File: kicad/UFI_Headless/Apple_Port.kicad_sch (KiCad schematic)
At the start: 28 parts, among them J14 DISK_II, J19 SYNC_SENSOR, J23 MAC_3.5_PORT, U16 SN74AHCT244PWR, U17 74LVC2G17GW, U18 ICL7662EBA+T, U26 74LVC14AD, U27 SN74AHCT244PWR

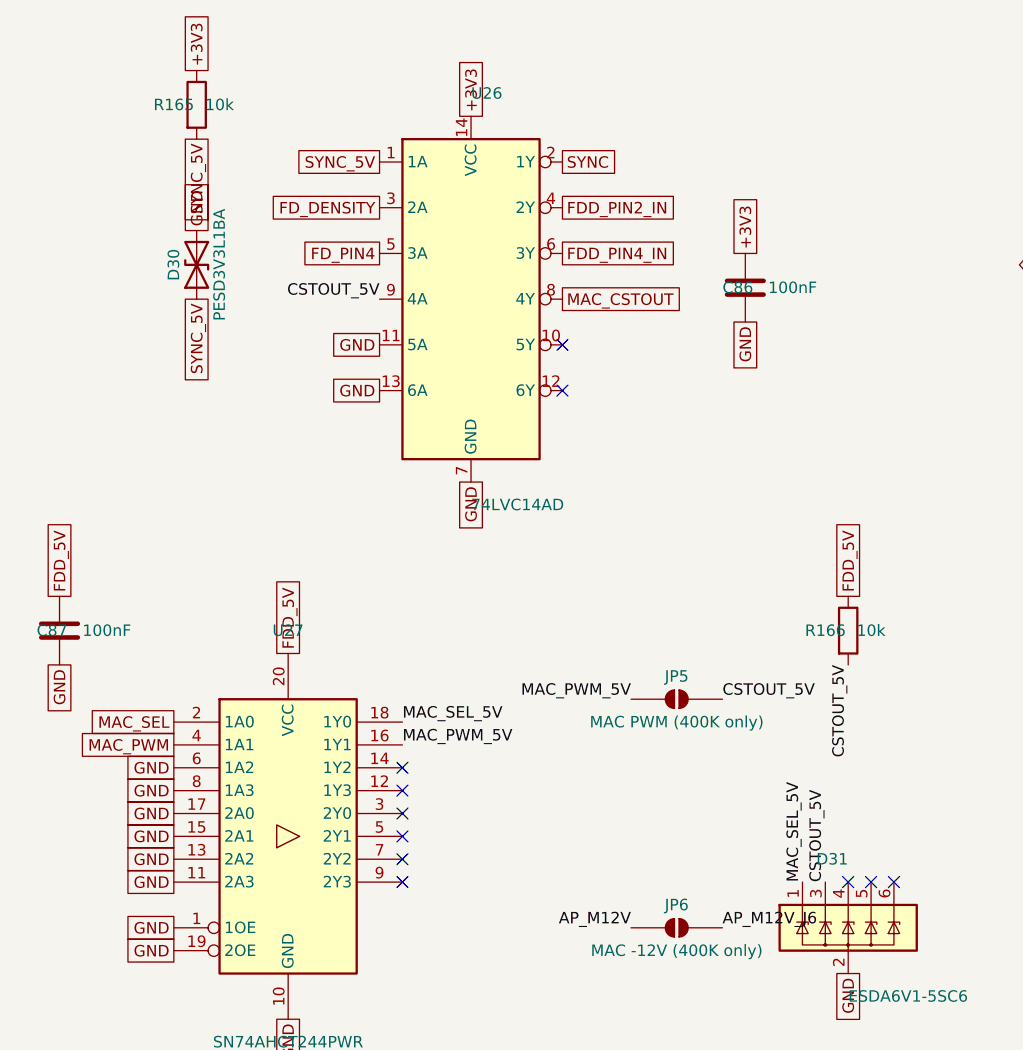
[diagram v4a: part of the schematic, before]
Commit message: KiCad v0.7 rework, stage A11f (fixes from the A8 review, owner decisions of 2026-10-25): F1 - the write gate is now hard-gated by a NOR instead of the A11a OR that had driven the MOSFET gate the wrong way since A11b: new U31 74LVC1G02 (MDD 74LVC1G02GW C52953351, SOT-353) on Flux_Interface forms Q9 gate = NOR(WGATE_n, LOCK), PE14 becomes WGATE_n (active low on every board revision again) with R167 10k pull-up to +3V3 so reset and boot leave the gate released, C88 100 nF; U30 gate 1 retired (1A/1B on GND, 1Y no-connect), gate 2 still gates APL_WRREQ with LOCK; netlist: FDD_WGATE = U5.67 R167 U31.1 J21.7, FDD_WGATE_G = U31.4 Q9.2 R151 TP8, LOCK = U14.4 U30.6 U31.2. Firmware in the same commit: board.h bus_out_inverted() excludes PE14, board_headless.c latches PE14 high at start-up; truth table for every MOSFET-driven line (reset / idle / active) recorded in PLAN.md, measurement point "J6 pin 24 stays high with the lock set during a read" in the README row, self-test item planned for A10; protocol doc (one hunk in the board_status bit 0 note). R1: D30 removed, SYNC_5V protected by the 5 V channel IO3 of D31 ESDA6V1-5SC6, J19 becomes a keyed JST B3B-XH-A (C144394). R2: J20 GUARD becomes JST B4B-XH-A (C144395) with D32-D34 PESD3V3L1BA (C51450) on GUARD_OFF_J/ERR5_J/ERR12_J; note that the Guard board v0.2 gets a JST XH J3 too. R3: flippy divider kept at 2.4k/2.4k (C22940, Greaseweazle V4.1 compatible), JP7 default GND. ERC over the whole project 0 errors / 0 warnings (build/erc.rpt). ARM build 0 warnings; offline gate as reported in the stage log. PLAN.md (A11f, polarity table), kicad README (A11f row). PCB follows in B3.
Claude-Session: https://claude.ai/code/session_014MdzrcyXuayppPHbfEjUrw
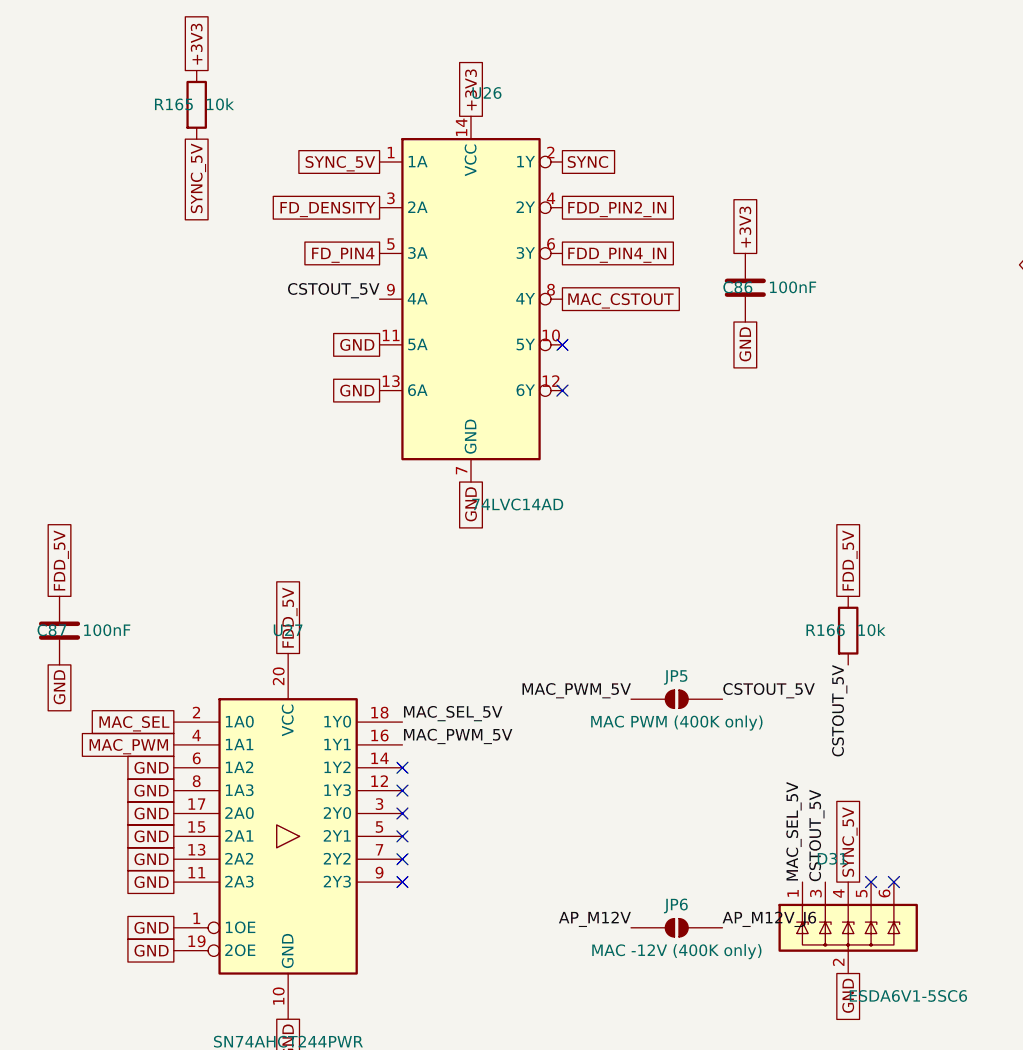
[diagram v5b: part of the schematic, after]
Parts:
- removed D30: PESD3V3L1BA, Diode_SMD:D_SOD-323, symbol Device:D_TVS
- J19: footprint Connector_PinHeader_2.54mm:PinHeader_1x03_P2.54mm_Vertical -> Connector_JST:JST_XH_B3B-XH-A_1x03_P2.50mm_Vertical; LCSC C49257 -> C144394; MPN (none) -> JST B3B-XH-A (sync sensor, keyed; A11f R1)
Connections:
- net SYNC_5V: now also D31.4 (IO3)
- no-connect marks 16 -> 15
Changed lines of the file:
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@@
 			)
 		)
-		(property "Footprint" "Connector_PinHeader_2.54mm:PinHeader_1x03_P2.54mm_Vertical"
+		(property "Footprint" "Connector_JST:JST_XH_B3B-XH-A_1x03_P2.50mm_Vertical"
 			(at 299.72 279.4 0)
 			(effects
@@
 			)
 		)
-		(property "LCSC" "C49257"
+		(property "LCSC" "C144394"
 			(at 299.72 279.4 0)
 			(effects
@@
 			)
 		)
+    (property "MPN" "JST B3B-XH-A (sync sensor, keyed; A11f R1)" (at 299.72 279.4 0)
+      (effects (font (size 1.27 1.27)) (hide yes))
+    )
 		(pin "1"
 		)
@@
 	)
 	(symbol
-		(lib_id "Device:D_TVS")
-		(at 190.5 276.86 90)
-		(unit 1)
-		(exclude_from_sim no)
-		(in_bom yes)
-		(on_board yes)
-		(dnp no)
-		(property "Reference" "D30"
-			(at 187.96 276.86 0)
-			(show_name no)
-			(do_not_autoplace no)
-			(effects
-				(font
-					(size 1.27 1.27)
-				)
-			)
-		)
-		(property "Value" "PESD3V3L1BA"
-			(at 193.04 276.86 0)
-			(show_name no)
-			(do_not_autoplace no)
-			(effects
-				(font
-					(size 1.27 1.27)
-				)
-			)
-		)
-		(property "Footprint" "Diode_SMD:D_SOD-323"
-			(at 190.5 276.86 0)
-			(hide yes)
-			(show_name no)
-			(do_not_autoplace no)
-			(effects
-				(font
-					(size 1.27 1.27)
-				)
-			)
-		)
-		(property "Datasheet" ""
-			(at 190.5 276.86 0)
-			(hide yes)
-			(show_name no)
-			(do_not_autoplace no)
-			(effects
-				(font
-					(size 1.27 1.27)
-				)
-			)
-		)
-		(property "Description" "Bidirectional transient-voltage-suppression diode"
-			(at 190.5 276.86 0)
-			(hide yes)
-			(show_name no)
-			(do_not_autoplace no)
-			(effects
-				(font
-					(size 1.27 1.27)
-				)
-			)
-		)
-		(property "MPN" "PESD3V3L1BA (same part as D28/D29)"
-			(at 190.5 276.86 0)
-			(effects
-				(font
-					(size 1.27 1.27)
-				)
-				(hide yes)
-			)
-		)
-		(pin "1"
-		)
-		(pin "2"
-		)
-		(instances
-			(project "UFI_Headless"
-				(path "/dc1b800d-cedf-5627-97f0-e6992ff33669/a4c7dd3a-3381-5fd0-85a1-c8054d9e8896"
-					(reference "D30")
-					(unit 1)
-				)
-			)
-		)
-	)
-	(symbol
 		(lib_id "Device:C")
 		(at 251.46 279.4 0)
@@
 			)
 			(justify right)
-		)
-	)
-	(global_label "SYNC_5V"
-		(at 190.5 280.67 270)
-		(effects
-			(font
-				(size 1.27 1.27)
-			)
-			(justify right)
-		)
-	)
-	(global_label "GND"
-		(at 190.5 273.05 90)
-		(effects
-			(font
-				(size 1.27 1.27)
-			)
-			(justify left)
 		)
 	)
@@
 			)
 		)
-    (property "LCSC" "C484743" (at 200.66 340.36 0)
-      (effects (font (size 1.27 1.27)) (hide yes))
-    )
-    (property "MPN" "TI SN74AHCT244PWR (Mac SEL / PWM level shift 3.3 -> 5 V, A11d K1)" (at 200.66 340.36 0)
-      (effects (font (size 1.27 1.27)) (hide yes))
-    )
+		(property "LCSC" "C484743"
+			(at 200.66 340.36 0)
+			(effects
+				(font
+					(size 1.27 1.27)
+				)
+				(hide yes)
+			)
+		)
+		(property "MPN" "TI SN74AHCT244PWR (Mac SEL / PWM level shift 3.3 -> 5 V, A11d K1)"
+			(at 200.66 340.36 0)
+			(effects
+				(font
+					(size 1.27 1.27)
+				)
+				(hide yes)
+			)
+		)
 		(pin "1"
 		)
@@
 			)
 		)
-    (property "MPN" "solder jumper, open: connects the PWM driver to pin 20 - only for a 400K drive (800K/FDHD drive !CSTOUT there)" (at 243.84 325.12 0)
-      (effects (font (size 1.27 1.27)) (hide yes))
-    )
+		(property "MPN" "solder jumper, open: connects the PWM driver to pin 20 - only for a 400K drive (800K/FDHD drive !CSTOUT there)"
+			(at 243.84 325.12 0)
+			(effects
+				(font
+					(size 1.27 1.27)
+				)
+				(hide yes)
+			)
+		)
 		(pin "1"
 		)
@@
 			)
 		)
-    (property "MPN" "solder jumper, open: -12 V to pin 9 - only for a 400K drive (800K/FDHD drive !EJECT there)" (at 243.84 350.52 0)
-      (effects (font (size 1.27 1.27)) (hide yes))
-    )
+		(property "MPN" "solder jumper, open: -12 V to pin 9 - only for a 400K drive (800K/FDHD drive !EJECT there)"
+			(at 243.84 350.52 0)
+			(effects
+				(font
+					(size 1.27 1.27)
+				)
+				(hide yes)
+			)
+		)
 		(pin "1"
 		)
@@
 			)
 		)
-    (property "MPN" "solder jumper, bridged: -12 V from U18 to Disk II J14 pin 9 (S5, no fuse: ICL7662 limits to about 20 mA)" (at 271.78 147.32 0)
-      (effects (font (size 1.27 1.27)) (hide yes))
-    )
+		(property "MPN" "solder jumper, bridged: -12 V from U18 to Disk II J14 pin 9 (S5, no fuse: ICL7662 limits to about 20 mA)"
+			(at 271.78 147.32 0)
+			(effects
+				(font
+					(size 1.27 1.27)
+				)
+				(hide yes)
+			)
+		)
 		(pin "1"
 		)
@@
 			)
 		)
-    (property "LCSC" "C25804" (at 262.89 317.5 0)
-      (effects (font (size 1.27 1.27)) (hide yes))
-    )
+		(property "LCSC" "C25804"
+			(at 262.89 317.5 0)
+			(effects
+				(font
+					(size 1.27 1.27)
+				)
+				(hide yes)
+			)
+		)
 		(pin "1"
 		)
@@
 			)
 		)
-    (property "LCSC" "C14663" (at 175.26 317.5 0)
-      (effects (font (size 1.27 1.27)) (hide yes))
-    )
+		(property "LCSC" "C14663"
+			(at 175.26 317.5 0)
+			(effects
+				(font
+					(size 1.27 1.27)
+				)
+				(hide yes)
+			)
+		)
 		(pin "1"
 		)
@@
 			)
 		)
-    (property "LCSC" "C6650" (at 262.89 350.52 0)
-      (effects (font (size 1.27 1.27)) (hide yes))
-    )
+		(property "LCSC" "C6650"
+			(at 262.89 350.52 0)
+			(effects
+				(font
+					(size 1.27 1.27)
+				)
+				(hide yes)
+			)
+		)
 		(pin "1"
 		)
@@
 			)
 		)
-    (property "LCSC" "C2977593" (at 299.72 335.28 0)
-      (effects (font (size 1.27 1.27)) (hide yes))
-    )
-    (property "MPN" "2x10 IDC header, Apple internal 20-pin floppy pinout (tashnotes): 1/3/5/7 GND, 2 CA0, 4 CA1, 6 CA2, 8 LSTRB, 10 !WRREQ, 12 SEL, 14 !ENBL, 16 RD, 18 WR, 11 +5V, 13/15/17/19 +12V, 9 -12V via JP6 (400K only), 20 PWM via JP5 (400K) / !CSTOUT input" (at 299.72 335.28 0)
-      (effects (font (size 1.27 1.27)) (hide yes))
-    )
+		(property "LCSC" "C2977593"
+			(at 299.72 335.28 0)
+			(effects
+				(font
+					(size 1.27 1.27)
+				)
+				(hide yes)
+			)
+		)
+		(property "MPN" "2x10 IDC header, Apple internal 20-pin floppy pinout (tashnotes): 1/3/5/7 GND, 2 CA0, 4 CA1, 6 CA2, 8 LSTRB, 10 !WRREQ, 12 SEL, 14 !ENBL, 16 RD, 18 WR, 11 +5V, 13/15/17/19 +12V, 9 -12V via JP6 (400K only), 20 PWM via JP5 (400K) / !CSTOUT input"
+			(at 299.72 335.28 0)
+			(effects
+				(font
+					(size 1.27 1.27)
+				)
+				(hide yes)
+			)
+		)
 		(pin "1"
 		)
@@
 	)
 	(no_connect
-		(at 262.89 345.44)
-	)
-	(no_connect
 		(at 265.43 345.44)
 	)
@@
 		)
 	)
+	(global_label "SYNC_5V"
+		(at 262.89 345.44 90)
+		(effects
+			(font
+				(size 1.27 1.27)
+			)
+			(justify left)
+		)
+	)

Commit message: KiCad v0.7 rework, stage C part 1 (BOM completion before the release, review note H12): every BOM row now carries an LCSC number, checked against the JLCPCB SMT catalogue on 2026-10-25 (stock in brackets). LAN sheet: U23 W5500 C32843 (9019), J22 HR911105A C12074 (72229, THT), Y2 25 MHz 12 pF +-10 ppm YXC X322525MOB4SI C9006 (basic; load capacitance 12 pF verified on the LCSC parameter page, fits the 18 pF C59/C60), C59/C60 18 pF C0G Yageo CC0603JRNPO9BN180 C107040, C61/C74 10 nF FH 0603B103K500NT C57112 (basic), C71 22 nF Samsung CL10B223KB8NNNC C21122 (basic), C72/C73 6.8 nF FH 0603B682K500NT C1631 (basic), C62 4.7 uF C1779, C63/C69 10 uF C15850, C64-C68/C70 100 nF C14663, FB2 C1002, R109 1M C22935, R111 12.4k 1 % C22865, R112/R113 49.9R 1 % C23185 (basic), R114 10R 1 % C22859 (basic), R115/R116 82R 1 % C23255, R117/R118 330R C23138, R119-R124 10k C25804. Other sheets: R75-R99/R105/R128 1k C21190, R74/R107/R108 10k C25804, R101-R104/R130 470R C23179, R106/R131 100k C25803, C58 100 nF C14663 (value text 100n -> 100nF so it groups with the other 100 nF), D18-D26/D28/D29 PESD3V3L1BA C51450 (48710) like D32-D34, Q5 2N7002 C8545 (basic), U22 TS5A3166DBVR C353035 (10678), J2 DC-005 2.0 C16214 (92305; same pin pattern as the KiCad BarrelJack_Horizontal footprint, placement to be checked in the JLC viewer), J7 2x12 IDC ZHOURI DC3-2.54-24PAS C5144580 (stock 81 - hand soldering stays the recommendation in docs/Bestellung_JLC.md), J12 2x8 IDC DC3-2.54-16PAS C2977594 (4335), J16 2x5 pin header XFCN PZ254V-12-10P C492422 (105667), J21 2x10 pin header PZ254V-12-20P C492427 (63622). Solder jumpers JP5-JP8 are excluded from the BOM (in_bom no) like JP1/JP3 - bare copper, nothing to place. Stock of the review's watch list: U9 SN74LS07DR C371970 4776, D31 ESDA6V1-5SC6 C6650 3010, L1 SRN6045TA-150M C1330797 1866. BOM export (kicad-cli sch export bom, grouped by value/footprint/LCSC): 99 rows, 0 without LCSC, 0 DNP. ERC over the whole project 0 errors / 0 warnings (build/erc.rpt). No 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
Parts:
- JP5, JP6, JP8: now left out of the parts list
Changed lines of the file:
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@@
 		(unit 1)
 		(exclude_from_sim no)
-		(in_bom yes)
+		(in_bom no)
 		(on_board yes)
 		(dnp no)
@@
 		(unit 1)
 		(exclude_from_sim no)
-		(in_bom yes)
+		(in_bom no)
 		(on_board yes)
 		(dnp no)
@@
 		(unit 1)
 		(exclude_from_sim no)
-		(in_bom yes)
+		(in_bom no)
 		(on_board yes)
 		(dnp no)
